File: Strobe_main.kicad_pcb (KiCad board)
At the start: 4 copper layers, 100 x 100 mm, 167 parts, among them J1001 Header, J302 T44007, J303 T44007, J304 10146581-060_M, J305 T44007, J306 T44007, J701 ZHOURI DC3, J800 Molex 430451227, J901 Header, Q100 MDT7N65, Q301 MPF3N150, Q303 IXYH55N120, Q304 IXYH55N120, Q305 IXYH55N120, U100 LM217MDT, U101 AMS1117-3.3, U102 AMS1117-3.3, U301 IRS2184, U401 TSV912IDT, U501 STM32G431K8Tx, U601 ISO1541, U602 ISO6741, Y501 20 MHz

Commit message: TP placement candidate 90%
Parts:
- removed R701, R702: 0R, Resistor_SMD:R_1206_3216Metric_Pad1.30x1.75mm_HandSolder
- added H100: MountingHole_Pad, MountingHole:MountingHole_3.2mm_M3_DIN965_Pad_TopBottom, F.Cu at (164.7, 55.5)
- C304, D402, Q301, R309, R311, R313, R316: moved to B.Cu
- D304, R319: moved to F.Cu
- R324: footprint Resistor_THT:R_Axial_DIN0617_L17.0mm_D6.0mm_P20.32mm_Horizontal -> Resistor_THT:R_Axial_DIN0617_L17.0mm_D6.0mm_P7.62mm_Vertical
- moved TP309 173.5 mm to (234.1, 21.0)
- moved Q301 134.3 mm to (230.0, 65.0)
- moved D309 133.8 mm to (205.0, 60.0), turned to 90 degrees
- moved R319 132.7 mm to (224.5, 65.0)
- moved D303 132.5 mm to (224.5, 65.0)
- moved R331 131.7 mm to (221.5, 61.0), turned to 0 degrees
- moved C309 130.7 mm to (208.0, 60.9), turned to 90 degrees
- moved D305 125.2 mm to (205.0, 67.0), turned to 90 degrees
- moved C307 124.3 mm to (208.0, 66.0), turned to 90 degrees
- moved R330 122.5 mm to (220.0, 66.5), turned to 90 degrees
- moved R324 122.2 mm to (243.5, 64.0), turned to 180 degrees
- moved R323 119.3 mm to (240.0, 69.5)
- moved R328 114.6 mm to (240.0, 75.0), turned to -90 degrees
- moved R329 110.2 mm to (238.5, 79.0), turned to 0 degrees
- moved TP303 64.9 mm to (203.7, 89.0), turned to -90 degrees
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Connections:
- J701 pad 2: Net-(J701-Pin_2) -> Earth
- J701 pad 4: Net-(J701-Pin_2) -> Earth
- J800 pad 1: /Block Diagram/S1k -> unconnected-(J800-Pin_1-Pad1)
- J800 pad 10: /Block Diagram/Vbus_ctrl -> /Block Diagram/SH0
- J800 pad 11: unconnected-(J800-Pin_11-Pad11) -> /Block Diagram/SH5
- J800 pad 12: unconnected-(J800-Pin_12-Pad12) -> /Block Diagram/Vbus_ctrl
- J800 pad 7: unconnected-(J800-Pin_7-Pad7) -> /Block Diagram/S1k
- J800 pad 9: /Block Diagram/SH5 -> unconnected-(J800-Pin_9-Pad9)
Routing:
- net Net-(R309-Pad1): track 0.00 -> 41.1 mm
- net /Block Diagram/SH20: track 72.7 -> 34.5 mm
- net /Block Diagram/Lamp driver/TP_REF: track 2.81 -> 25.7 mm, vias 0 -> 2
- net Net-(J701-Pin_2): track 18.9 -> 0.00 mm
- net /Block Diagram/S1k: track 60.3 -> 75.6 mm
- net Earth: track 0.00 -> 13.5 mm
- net /Block Diagram/Lamp driver/DRV_OUT: track 68.8 -> 55.3 mm
- net /Block Diagram/Lamp driver/G_L_D3: track 0.00 -> 9.34 mm
- net /Block Diagram/Optical isolation/LV_SWDIO: track 17.5 -> 24.9 mm
- net /Block Diagram/SH0: track 45.0 -> 37.8 mm
- net /Block Diagram/Lamp driver/TRIG: track 0.00 -> 7.12 mm
- net /Block Diagram/Lamp driver/G_L_D_2: track 2.80 -> 9.83 mm
- net /Block Diagram/Lamp driver/G_L_D1: track 2.80 -> 9.83 mm
- net /Block Diagram/Lamp driver/LMP: track 0.00 -> 6.00 mm
- net /Block Diagram/Lamp driver/Mon_IL: track 21.2 -> 27.1 mm
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
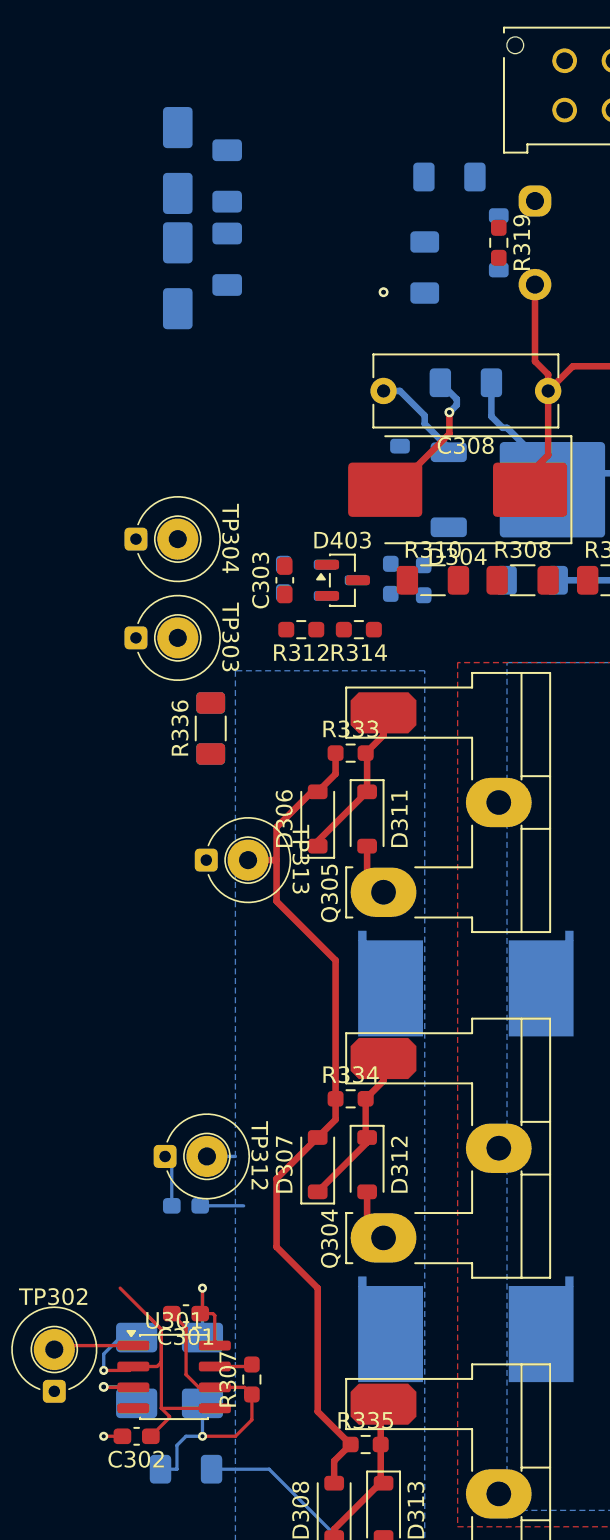
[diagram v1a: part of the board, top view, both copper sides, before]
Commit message: Updated some clearance rules
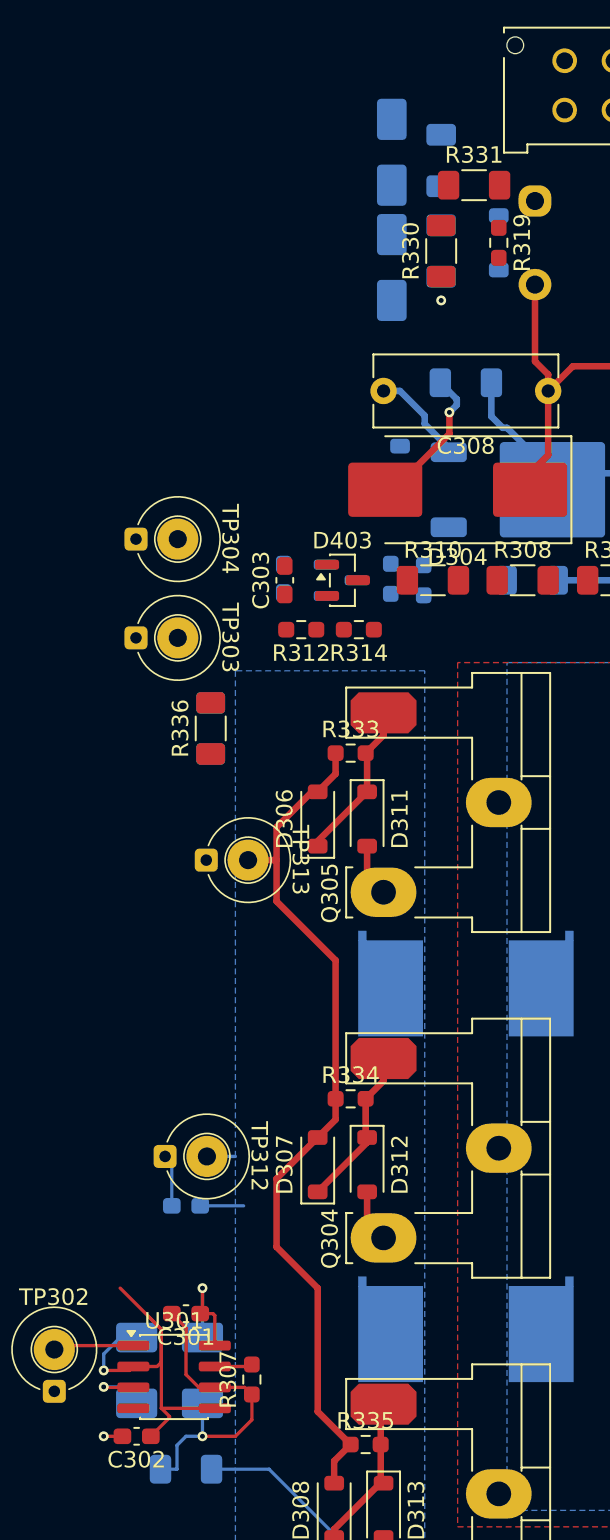
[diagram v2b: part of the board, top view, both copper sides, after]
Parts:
- R330, R331: moved to F.Cu
- moved C309 13.0 mm to (221.0, 60.0)
- moved C307 13.0 mm to (221.0, 65.5)
- moved D305 13.0 mm to (218.0, 66.5)
- moved D309 13.0 mm to (218.0, 59.5)
- moved R331 1.58 mm to (223.0, 61.5)
- moved R330 1.41 mm to (221.0, 65.5)
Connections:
- net Net-(D305-A) renamed /Block Diagram/Lamp driver/REF_M
- net Net-(R330-Pad2) renamed /Block Diagram/Lamp driver/TP_RM
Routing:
- net /Block Diagram/Lamp driver/TP_REF: track 25.7 -> 22.0 mm

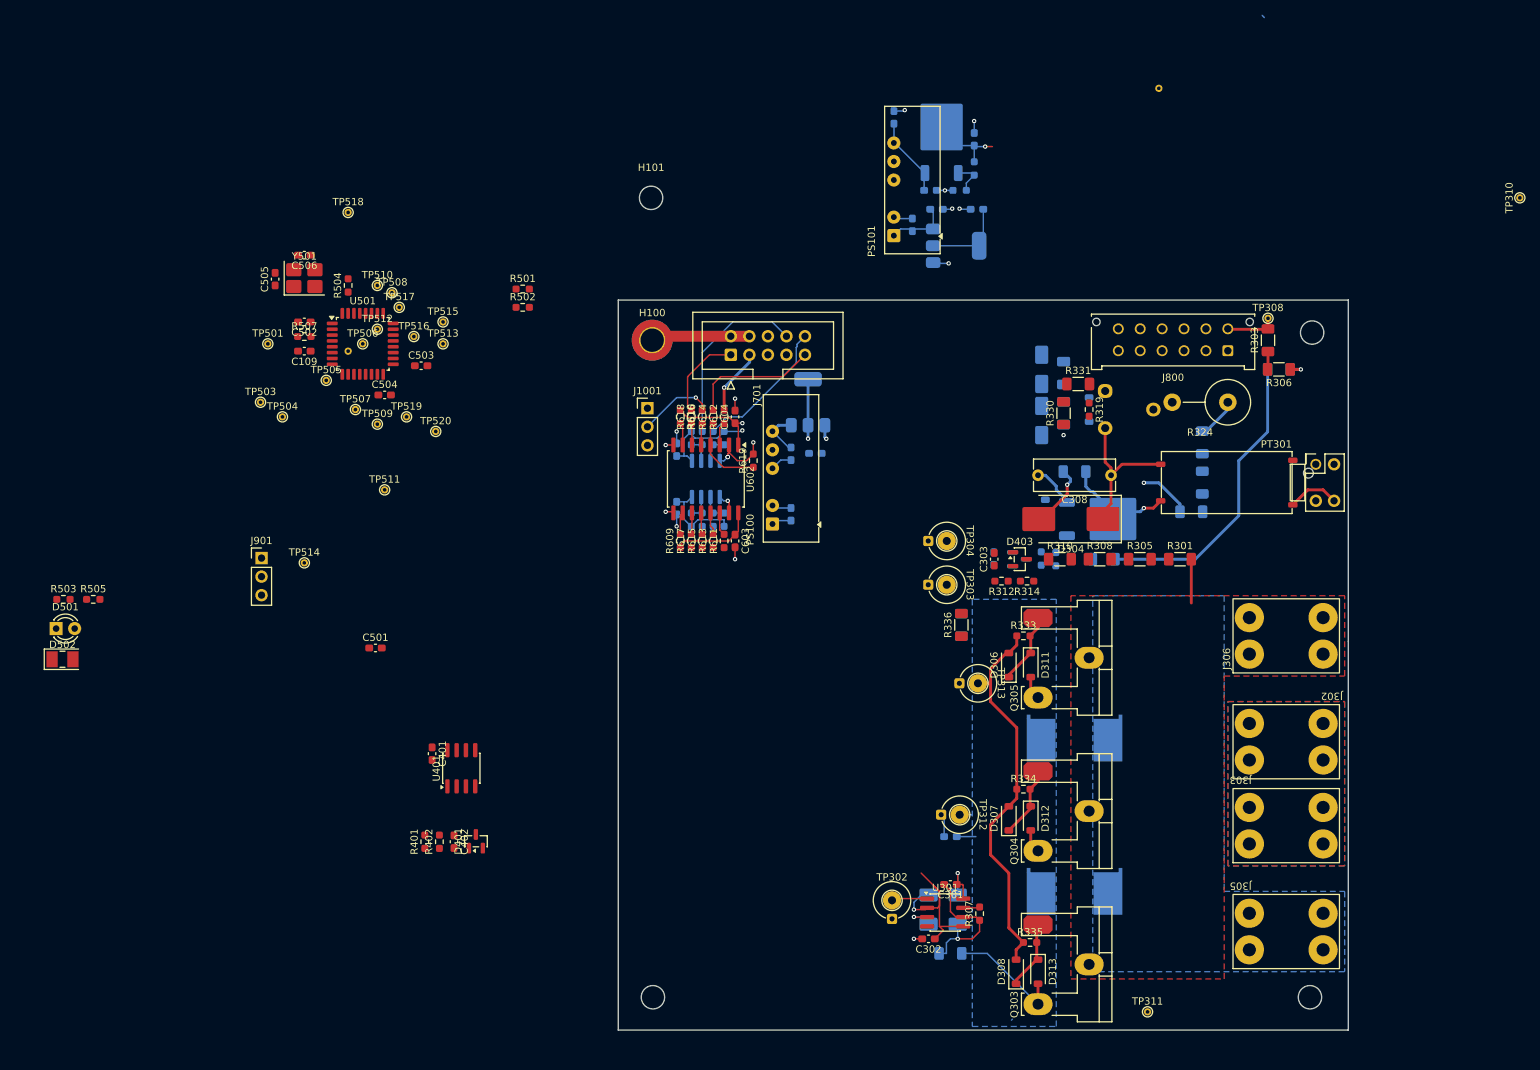
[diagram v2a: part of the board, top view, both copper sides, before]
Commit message: Placement complplete, feasibility routing complete
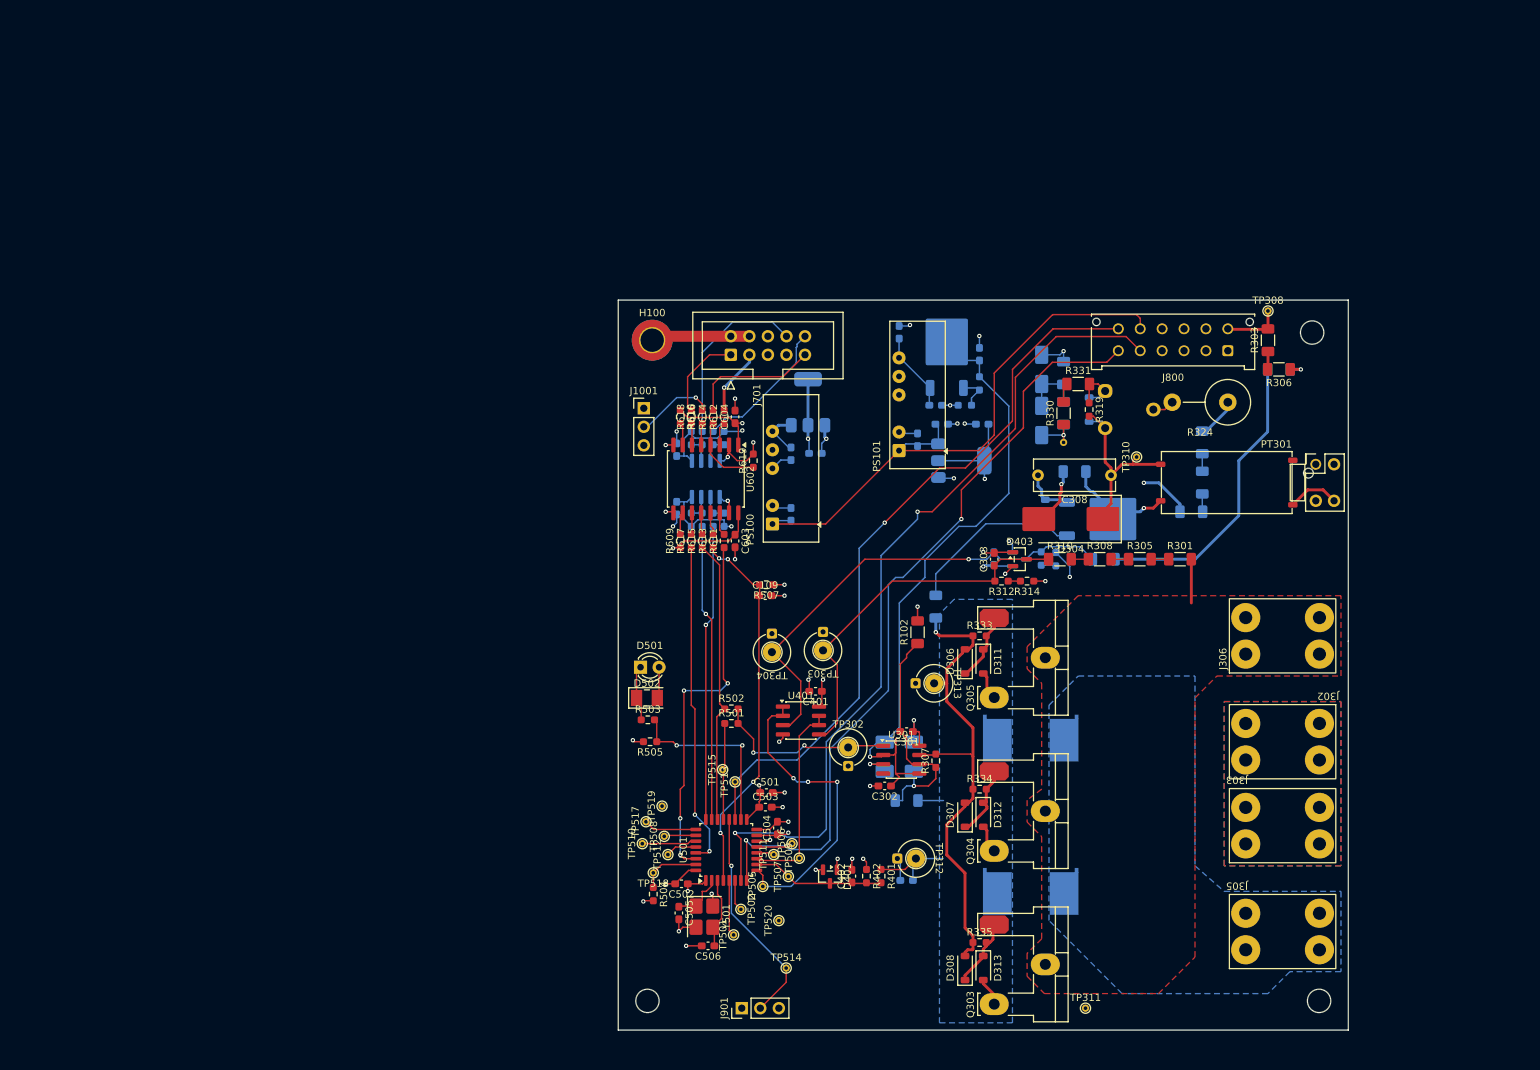
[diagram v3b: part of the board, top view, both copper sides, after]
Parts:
- removed H101: MountingHole, MountingHole:MountingHole_3.2mm_M3
- removed TP503, TP504, TP516: TestPoint, TestPoint:TestPoint_THTPad_D1.0mm_Drill0.5mm
- R102, TP502: moved to F.Cu
- R336: moved to B.Cu
- moved C506 109.6 mm to (172.3, 138.5)
- moved Y501 103.2 mm to (171.8, 134.5), turned to -90 degrees
- moved TP501 103.1 mm to (175.8, 137.0), turned to 90 degrees
- moved C505 102.9 mm to (168.3, 134.0), turned to -90 degrees
- moved TP518 99.7 mm to (164.8, 128.5), turned to 180 degrees
- moved TP502 93.5 mm to (176.8, 133.5), turned to -90 degrees
- moved R504 93.3 mm to (164.8, 131.4), turned to -90 degrees
- moved C502 92.7 mm to (168.7, 130.0)
- moved TP505 91.6 mm to (179.8, 130.3), turned to 90 degrees
- moved TP506 90.2 mm to (183.8, 124.5), turned to 90 degrees
- moved J901 90.2 mm to (176.9, 147.0), turned to 90 degrees
- moved TP507 87.2 mm to (183.3, 129.0), turned to 90 degrees
- moved TP514 86.2 mm to (183.0, 141.5)
- moved U501 85.4 mm to (174.8, 125.3), turned to 90 degrees
- moved TP510 84.6 mm to (163.3, 124.5), turned to 90 degrees
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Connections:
- U501 pad 22: Net-(U501-PA12) -> /Block Diagram/MCU/HV_EXT_EN
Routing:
- net /Block Diagram/MCU/SUP_TX: track 0.00 -> 114.0 mm, vias 0 -> 2
- net /Block Diagram/MCU/SUP_RX: track 0.00 -> 106.5 mm, vias 0 -> 2
- net /Block Diagram/Vbus_ctrl: track 0.00 -> 99.5 mm, vias 0 -> 1
- net /Block Diagram/SH5: track 11.9 -> 80.7 mm
- net /Block Diagram/Lamp driver/Mon_S1k: track 0.00 -> 64.6 mm, vias 0 -> 1
- net /Block Diagram/SH0: track 37.8 -> 99.3 mm, vias 12 -> 34
- net /Block Diagram/SH20: track 34.5 -> 87.6 mm, vias 2 -> 1
- net /Block Diagram/MCU/HV_NRST: track 0.00 -> 51.7 mm, vias 0 -> 4
- net /Block Diagram/Lamp driver/Mon_LMP: track 0.00 -> 51.4 mm
- net /Block Diagram/MCU/HV_RX: track 0.00 -> 50.3 mm, vias 0 -> 4
- net /Block Diagram/MCU/HV_TX: track 0.00 -> 44.6 mm, vias 0 -> 2
- net /Block Diagram/MCU/Mon_S1k_buf: track 0.00 -> 42.8 mm, vias 0 -> 3
- net /Block Diagram/MCU/HV_SWDIO: track 0.00 -> 40.7 mm, vias 0 -> 1
- net /Block Diagram/MCU/HV_SWDCLK: track 0.00 -> 40.6 mm, vias 0 -> 1
- net /Block Diagram/MCU/HV_EXT_EN: track 0.00 -> 39.0 mm
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- added copper zone on In1.Cu, net /Block Diagram/Lamp driver/LMP
- added copper zone on In2.Cu, net /Block Diagram/Lamp driver/LMP
- added copper zone on In2.Cu, net /Block Diagram/SH0
- added copper zone on In2.Cu, net /Block Diagram/SH3

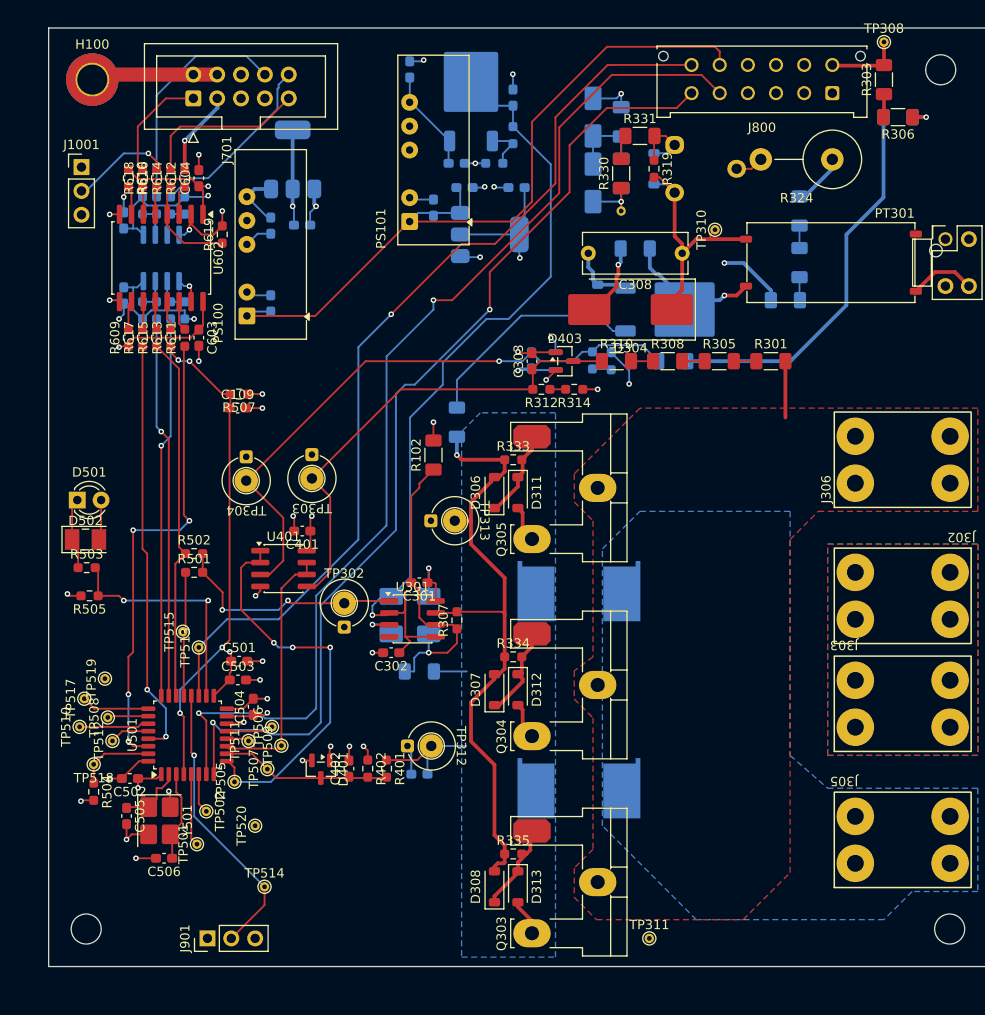
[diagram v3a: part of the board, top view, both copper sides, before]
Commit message: MCU routed
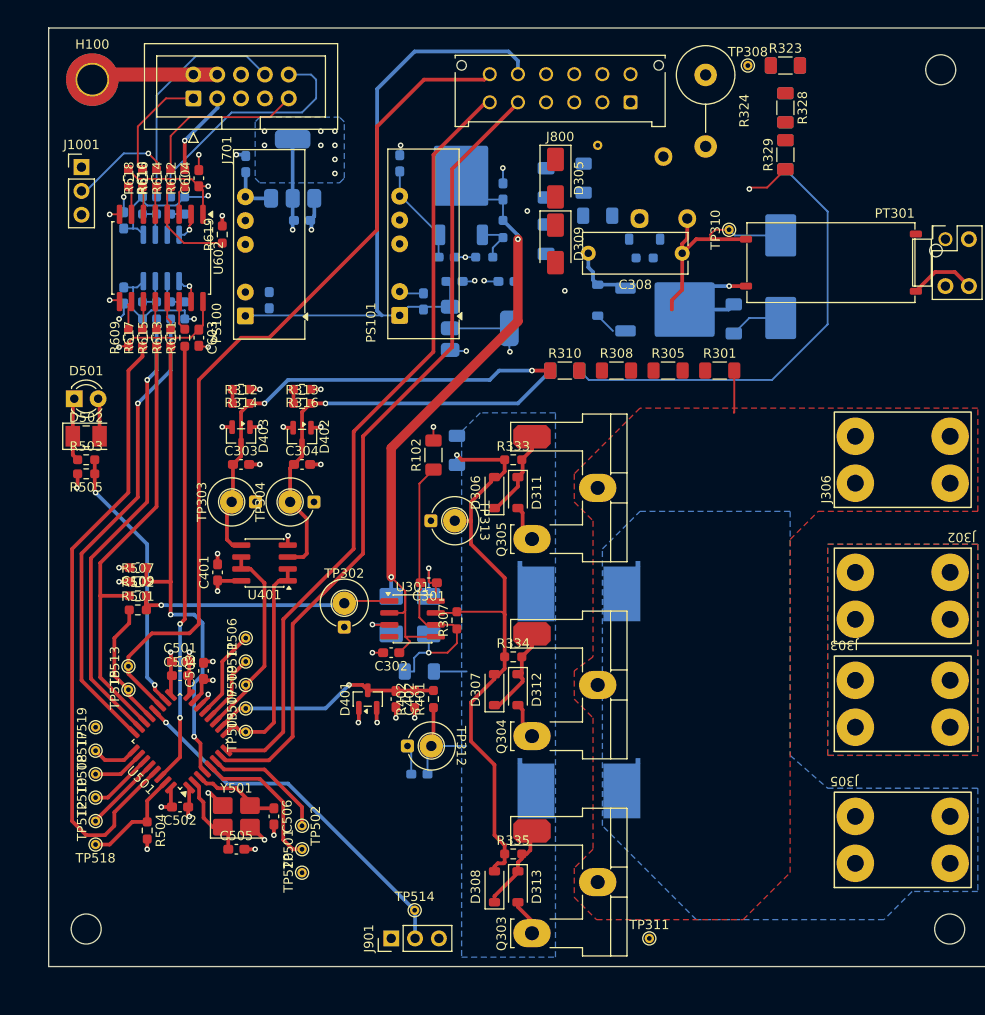
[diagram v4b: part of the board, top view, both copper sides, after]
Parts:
- C304, D305, D309, D402, R313, R316, R323, R328, R329: moved to F.Cu
- D304, R303, R306, R319, R330, R331: moved to B.Cu
- moved R314 35.5 mm to (180.5, 88.5)
- moved D403 35.4 mm to (180.5, 93.5), turned to -90 degrees
- moved R316 33.1 mm to (187.0, 88.5), turned to 180 degrees
- moved C303 32.9 mm to (180.5, 96.5), turned to 0 degrees
- moved R312 32.0 mm to (180.5, 90.0), turned to 0 degrees
- moved R313 31.3 mm to (187.0, 90.0), turned to 0 degrees
- moved D402 29.1 mm to (187.0, 93.5), turned to -90 degrees
- moved C304 26.8 mm to (187.0, 96.5), turned to 0 degrees
- moved R507 22.7 mm to (169.5, 109.0), turned to 0 degrees
- moved J800 21.5 mm to (222.0, 57.9)
- moved C109 20.1 mm to (169.5, 107.5), turned to 180 degrees
- moved J901 19.6 mm to (196.5, 147.0)
- moved R328 16.6 mm to (238.5, 58.5)
- moved D304 16.4 mm to (238.0, 76.5), turned to -90 degrees
- moved R324 16.2 mm to (230.0, 55.0), turned to -90 degrees
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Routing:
- net /Block Diagram/MCU/SUP_TX: track 114.0 -> 86.4 mm, vias 2 -> 0
- net /Block Diagram/SH0: track 99.3 -> 72.7 mm, vias 34 -> 36
- net /Block Diagram/MCU/SUP_RX: track 106.5 -> 83.3 mm, vias 2 -> 0
- net /Block Diagram/MCU/HV_TX: track 44.6 -> 66.8 mm, vias 2 -> 0
- net /Block Diagram/Lamp driver/G_TP_DRV: track 24.5 -> 2.31 mm
- net /Block Diagram/MCU/Mon_S1k_buf: track 42.8 -> 23.4 mm, vias 3 -> 0
- net /Block Diagram/Lamp driver/Mon_S1k: track 64.6 -> 46.8 mm
- net /Block Diagram/SH20: track 87.6 -> 70.7 mm, vias 1 -> 2
- net /Block Diagram/SH5: track 80.7 -> 68.4 mm
- net /Block Diagram/MCU/HV_SWDCLK: track 40.6 -> 50.3 mm
- net /Block Diagram/Lamp driver/TP_REF: track 33.4 -> 23.6 mm, vias 2 -> 1
- net /Block Diagram/Light_sns: track 30.5 -> 39.5 mm
- net Net-(U501-PA1): track 4.29 -> 13.2 mm
- net /Block Diagram/MCU/HV_EXT_EN: track 39.0 -> 47.5 mm
- net /Block Diagram/Lamp driver/REF_M: track 8.40 -> 0.00 mm, vias 0 -> 1
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- added copper zone on B.Cu, net /Block Diagram/SL3
